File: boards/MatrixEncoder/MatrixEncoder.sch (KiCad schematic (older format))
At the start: 14 parts

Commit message: Added first matrix encoder schematics, some design files
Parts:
- removed P?: CONN_5X2, symbol CONN_5X2
- removed U? (x8): 74LS151, ~, symbol 74LS151
- added P?: CONN_8X2, symbol CONN_8X2
- added R? (x26): 10k, ~, symbol R
- added RR? (x12): 8x10k, ~, symbol RR8
- added U? (x2): 74LS153, ~, symbol 74LS153
- added U? (x15): 74LS151, ~, symbol 74LS151
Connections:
- net labels added: a1, a10, a11, a12, a13, a14, a15, a16, a17, a18, a19, a2, a20, a3, a4, a5, a6, a7, a8, a9, b1, b11, b12, b13, b14, b15, b16, b17, b18, b19, b2, b20, b3, b4, b5, b6, b7, b8, b9, c1, c10, c11, c12, c13, c14, c15, c16, c17, c18, c19, c2, c20, c3, c4, c5, c6, c7, c8, c9, d1, d11, d12, d13, d14, d15, d16, d17, d18, d19, d2, d20, d3, d4, d5, d6, d7, d8, d9, e1, e10, e11, e12, e13, e14, e15, e16, e17, e18, e19, e2, e20, e3, e4, e5, e6, e7, e8, e9, f1, f11, f12, f13, f14, f15, f16, f17, f18, f19, f2, f20, f3, f4, f5, f6, f7, f8, f9, g1, g2, g3, g4, g5, s0, s1, s2, s3, s4
- net labels removed: VCC
- wire segments 5 -> 453
- no-connect marks 0 -> 3
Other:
- moved on the sheet: P?, U?

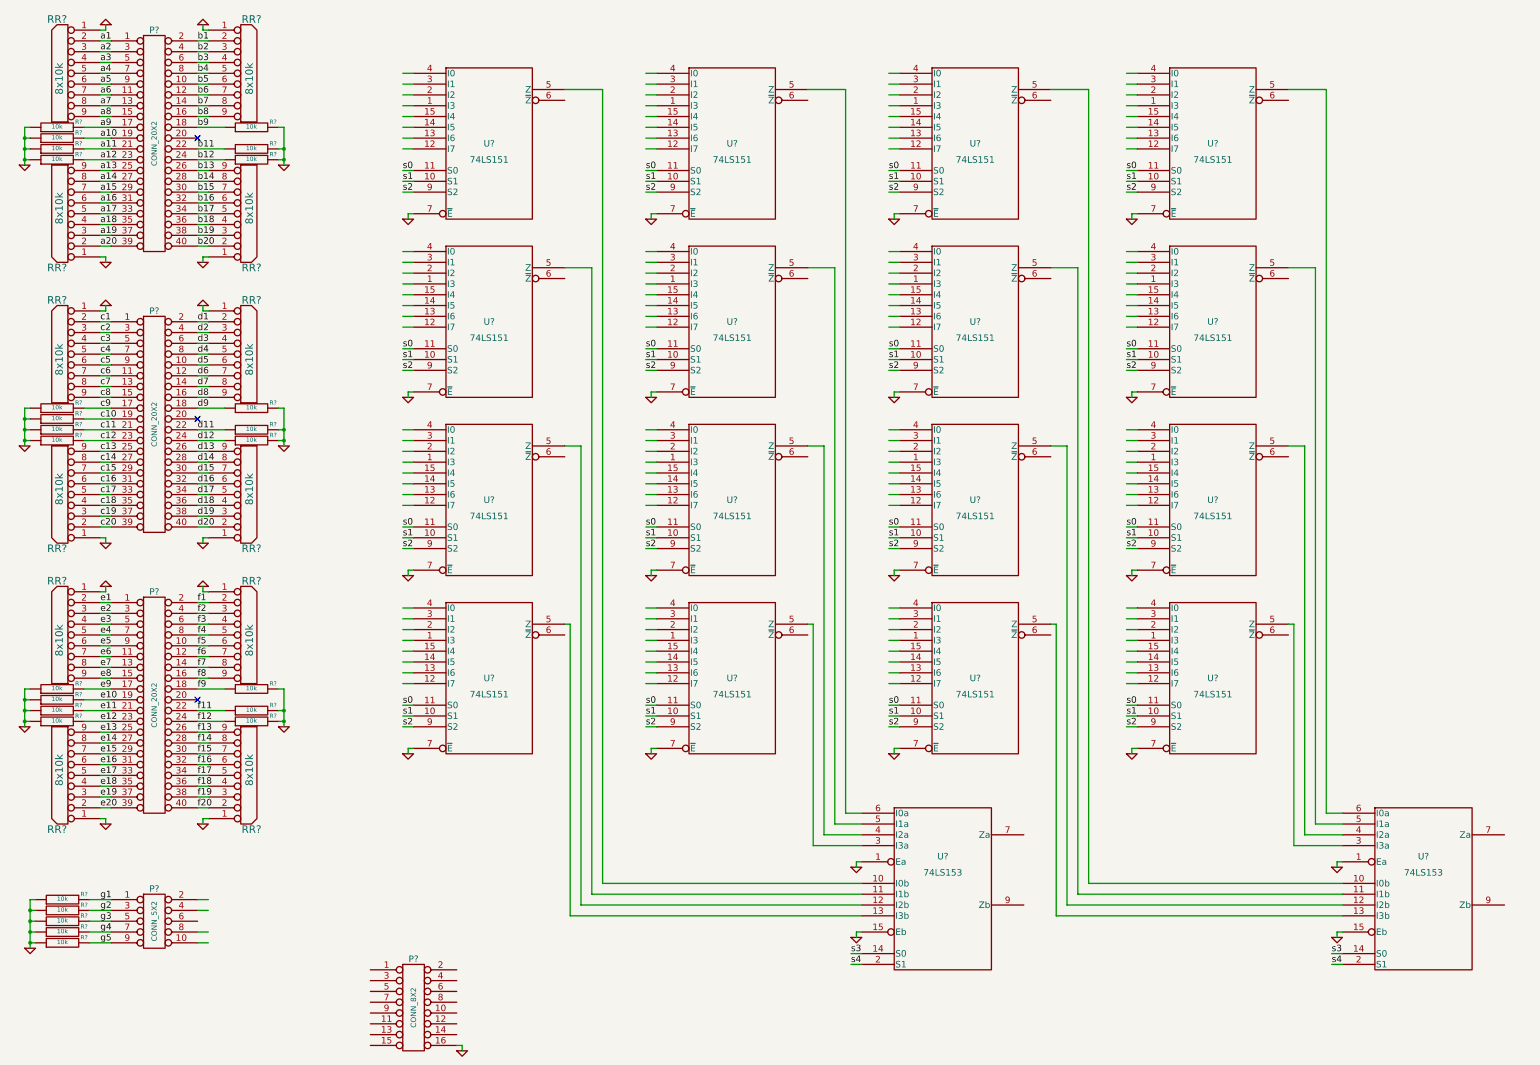
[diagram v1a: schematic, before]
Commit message: Updated matrix encoder schematics
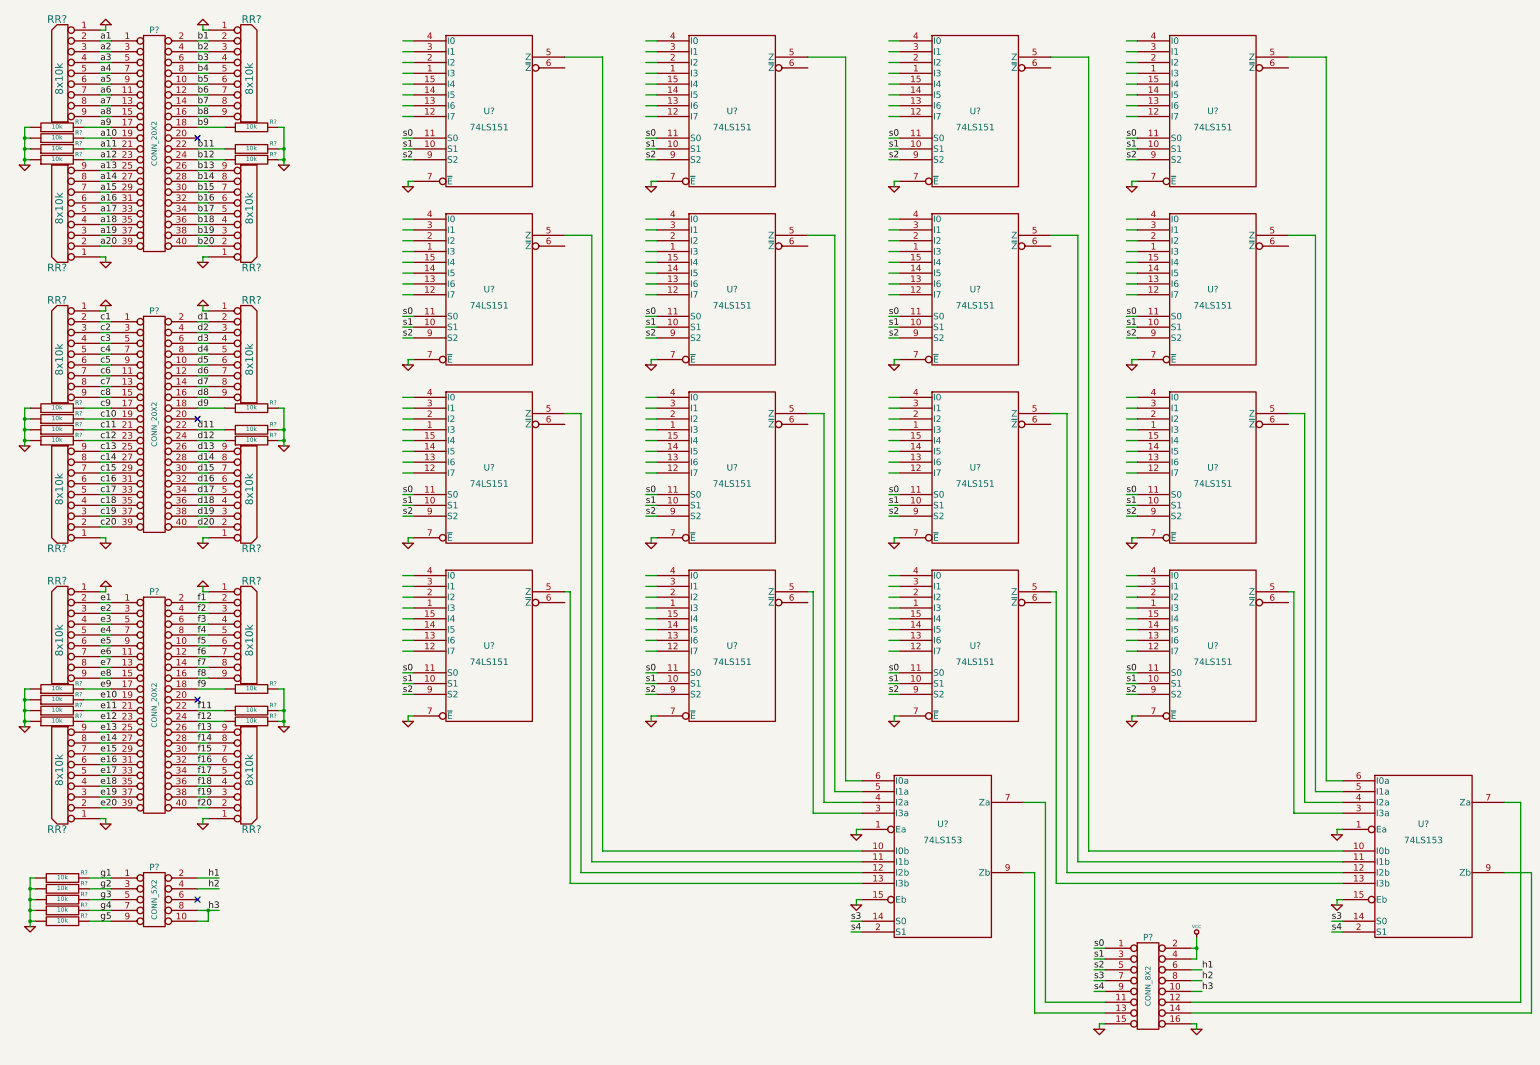
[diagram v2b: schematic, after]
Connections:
- net labels added: VCC, h1, h2, h3
- wire segments 453 -> 479
- no-connect marks 3 -> 4
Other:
- moved on the sheet: P?, R?, U?
